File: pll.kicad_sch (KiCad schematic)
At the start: 54 parts, among them J201 S353/CDP18U42P, Q201 DTC143ZE, Q202 DTC143ZE, Q203 DTC143ZE, Q204 DTC143ZE, Q205 DTC143ZE, Q206 DTC143ZE, Q207 DTC143ZE, Q208 DTC143ZE, Q209 DTC143ZE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

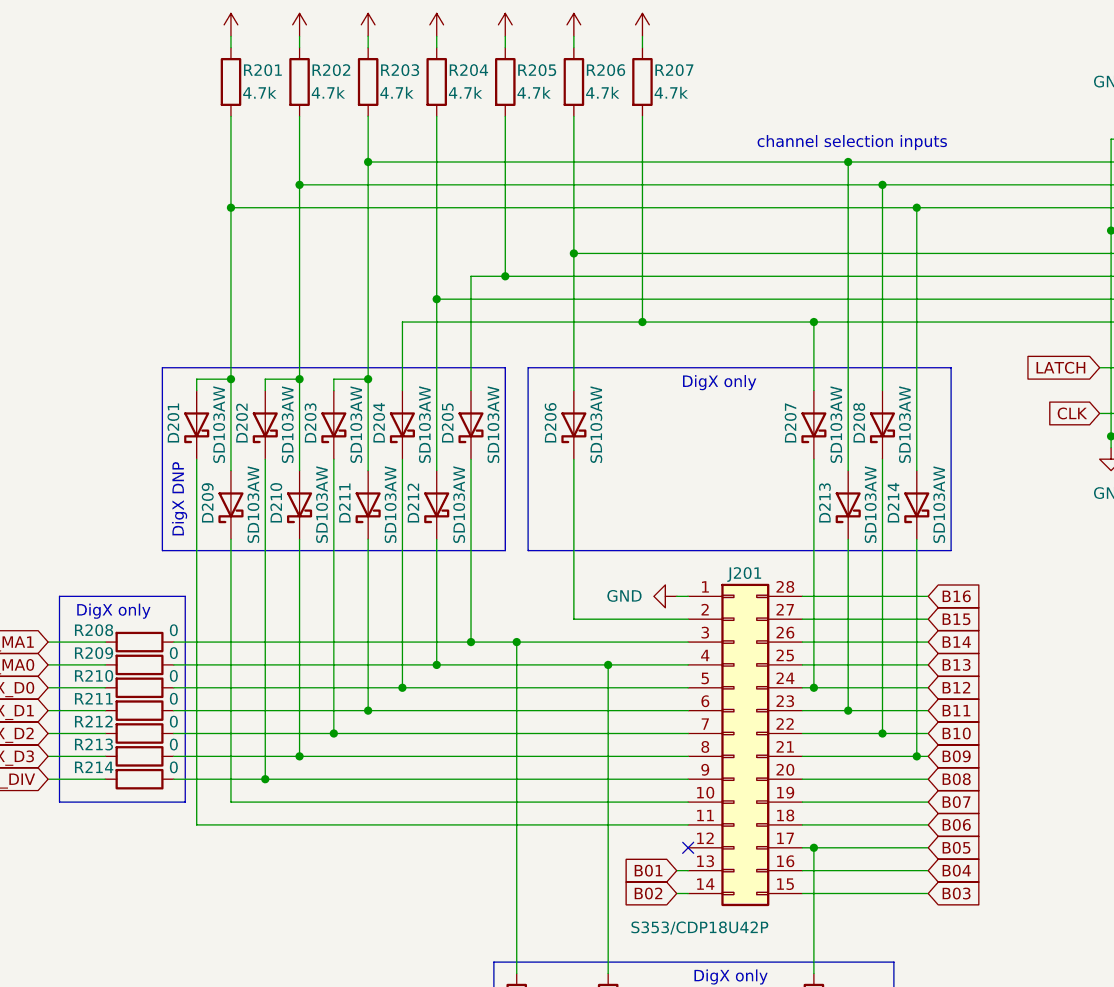
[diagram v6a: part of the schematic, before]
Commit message: silkscreen symbols and text, various schematic/pcb updates
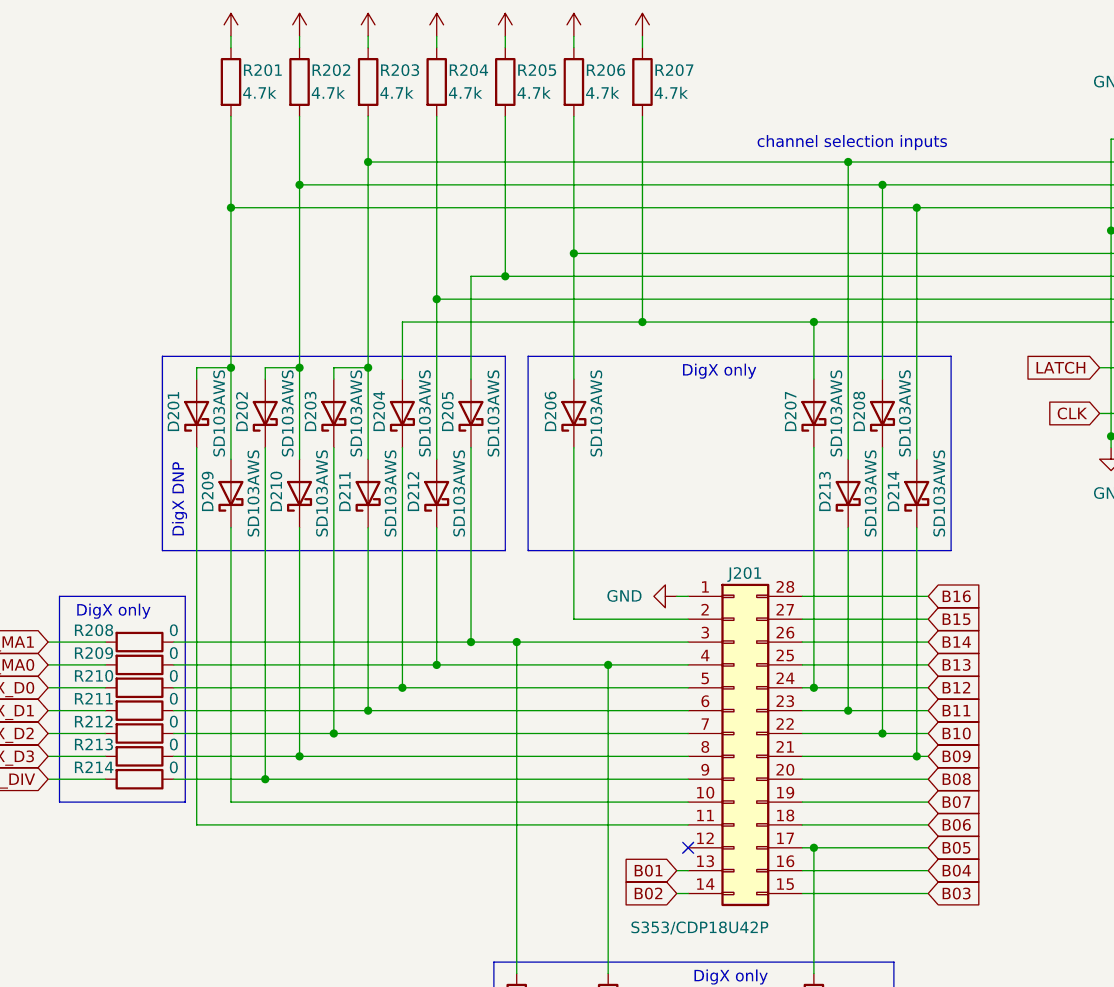
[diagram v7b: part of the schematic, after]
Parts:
- D201, D202, D203, D204, D205, D206, D207, D208, D209, D210, D211, D212, D213, D214: value SD103AW -> SD103AWS; footprint Diode_SMD:D_SOD-123 -> Diode_SMD:D_SOD-323; LCSC C181204 -> C438010
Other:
- moved on the sheet: D201, D202, D203, D204, D205, D206, D207, D208, D209, D210, D211, D212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
